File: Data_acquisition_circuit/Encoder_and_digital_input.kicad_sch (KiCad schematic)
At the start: 12 parts, among them U3 7414

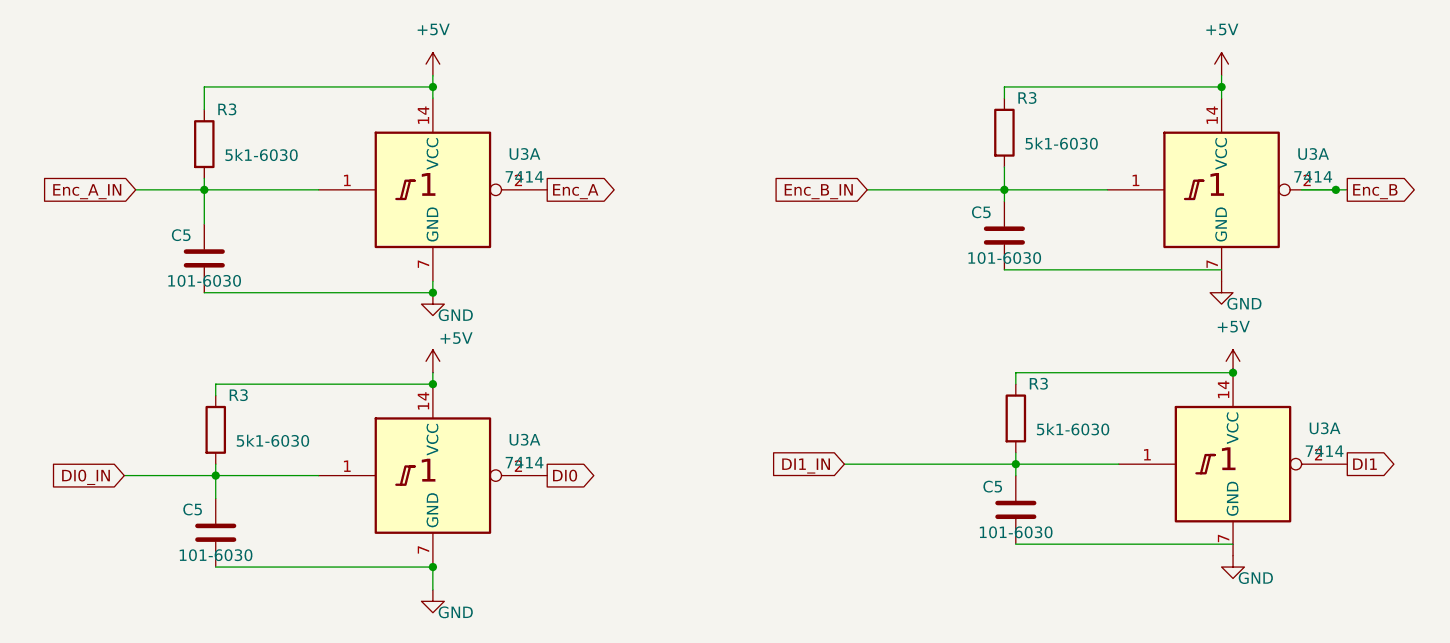
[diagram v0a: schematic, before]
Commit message: covert 0603 to 0805
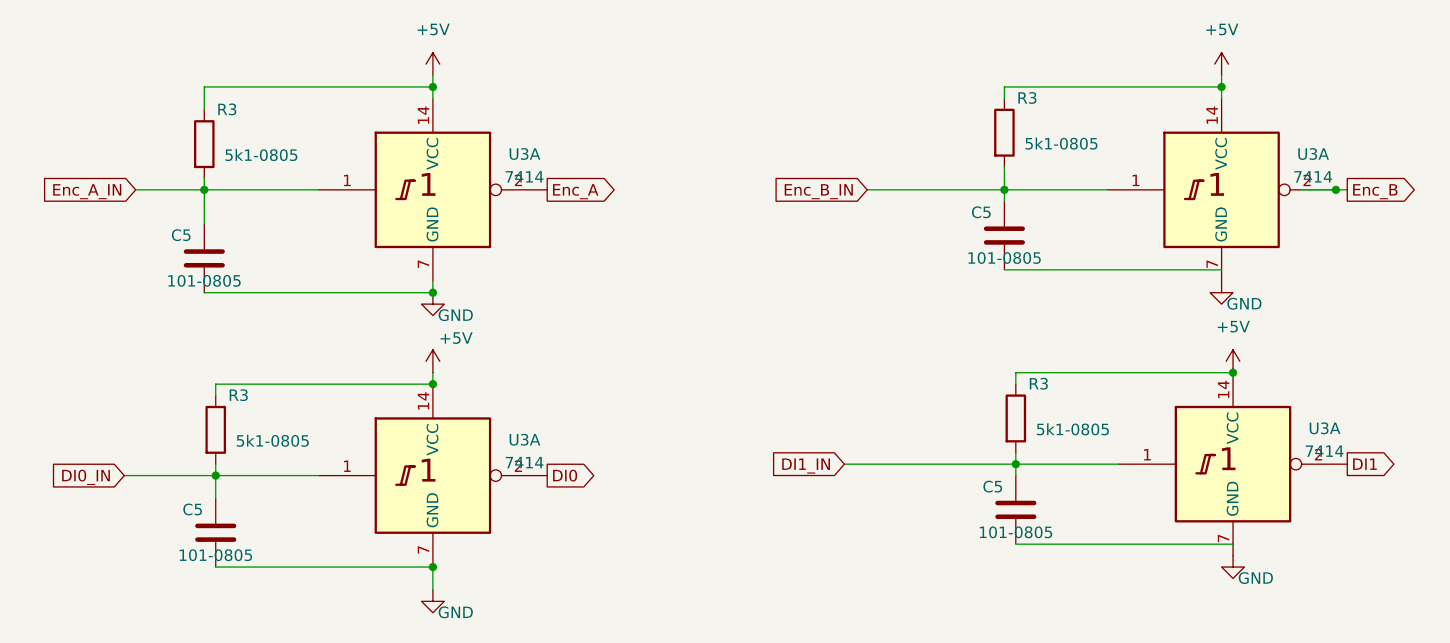
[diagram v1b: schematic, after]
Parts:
- C5: value 101-6030 -> 101-0805
- R3: value 5k1-6030 -> 5k1-0805
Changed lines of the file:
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@@
       (effects (font (size 1.27 1.27)))
     )
-    (property "Value" "5k1-6030" (at 83.82 64.77 0)
+    (property "Value" "5k1-0805" (at 83.82 64.77 0)
       (effects (font (size 1.27 1.27)))
     )
@@
       (effects (font (size 1.27 1.27)))
     )
-    (property "Value" "101-6030" (at 166.37 76.2 0)
+    (property "Value" "101-0805" (at 166.37 76.2 0)
       (effects (font (size 1.27 1.27)))
     )
@@
       (effects (font (size 1.27 1.27)))
     )
-    (property "Value" "101-6030" (at 167.64 106.68 0)
+    (property "Value" "101-0805" (at 167.64 106.68 0)
       (effects (font (size 1.27 1.27)))
     )
@@
       (effects (font (size 1.27 1.27)))
     )
-    (property "Value" "5k1-6030" (at 85.09 96.52 0)
+    (property "Value" "5k1-0805" (at 85.09 96.52 0)
       (effects (font (size 1.27 1.27)))
     )
@@
       (effects (font (size 1.27 1.27)))
     )
-    (property "Value" "101-6030" (at 78.74 109.22 0)
+    (property "Value" "101-0805" (at 78.74 109.22 0)
       (effects (font (size 1.27 1.27)))
     )
@@
       (effects (font (size 1.27 1.27)))
     )
-    (property "Value" "101-6030" (at 77.47 78.74 0)
+    (property "Value" "101-0805" (at 77.47 78.74 0)
       (effects (font (size 1.27 1.27)))
     )
@@
       (effects (font (size 1.27 1.27)))
     )
-    (property "Value" "5k1-6030" (at 172.72 63.5 0)
+    (property "Value" "5k1-0805" (at 172.72 63.5 0)
       (effects (font (size 1.27 1.27)))
     )
@@
       (effects (font (size 1.27 1.27)))
     )
-    (property "Value" "5k1-6030" (at 173.99 95.25 0)
-      (effects (font (size 1.27 1.27)))
-    )
+    (property "Value" "5k1-0805" (at 173.99 95.25 0)
+      (effects (font (size 1.27 1.27)))
+    )
